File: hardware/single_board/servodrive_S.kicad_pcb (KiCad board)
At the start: 6 copper layers, 65 x 65 mm, 194 parts, among them J1 PhasePad_Arc, J12 USB-C, J13 EXPANSION, J14 RS485 IN, J15 RS485 OUT, J2 PhasePad_Arc, J3 PhasePad_Arc, J4 XT30, Q1 BSC030N08NS5, Q1001 2N7002, Q2 BSC030N08NS5, Q3 BSC030N08NS5, Q4 BSC030N08NS5, Q5 BSC030N08NS5, Q6 BSC030N08NS5, SW1 BOOTSEL, U1 EG2103, U10 MT6701, U11 LMR38010SDDAR, U12 LMR38010SDDAR, U13 USBLC6-2SC6, U14 SIT3088ETK, U15 SIT3088ETK, U17 SIT3088ETK, U18 SIT3088ETK, U2 EG2103, U3 EG2103, U4 INA241A3, U5 INA241A3, U6 INA241A3, U7 RP2350A, U8 W25Q16JVUXIQ, U9 SPX3819M5-3.3, Y1 12MHz

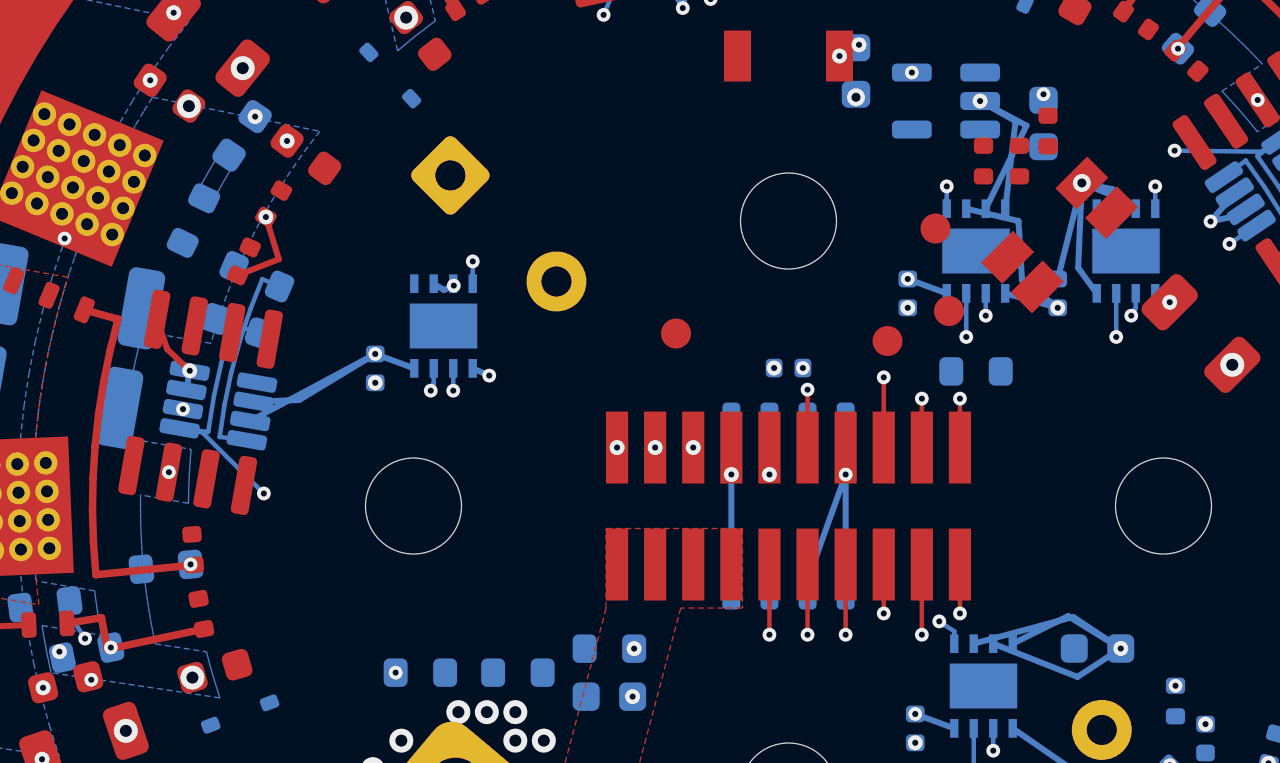
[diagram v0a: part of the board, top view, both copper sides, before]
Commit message: fanout.taps: no sliver where a pad joins a neighbour's tap
J13's pin swap put EXP_GP24 on the pad above the MT6701's pin 2, so
that pin lost its via-in-pad and linked to pin 1's tap via instead: two
+3V3 tracks meeting at 19.8 degrees, a copper sliver in KiCad's DRC.
A link that would arrive at a via at 2-20 degrees to a track running
from it to one of the net's pads now goes straight to that pad. On
board S that changes U10 pins 1-2 and one +3V3 pair at (157.8, 94.2)
(11.6 degrees); board A's fan-out is unchanged.

Co-Authored-By: Claude Opus 5.5 (1M context) <noreply@anthropic.com>
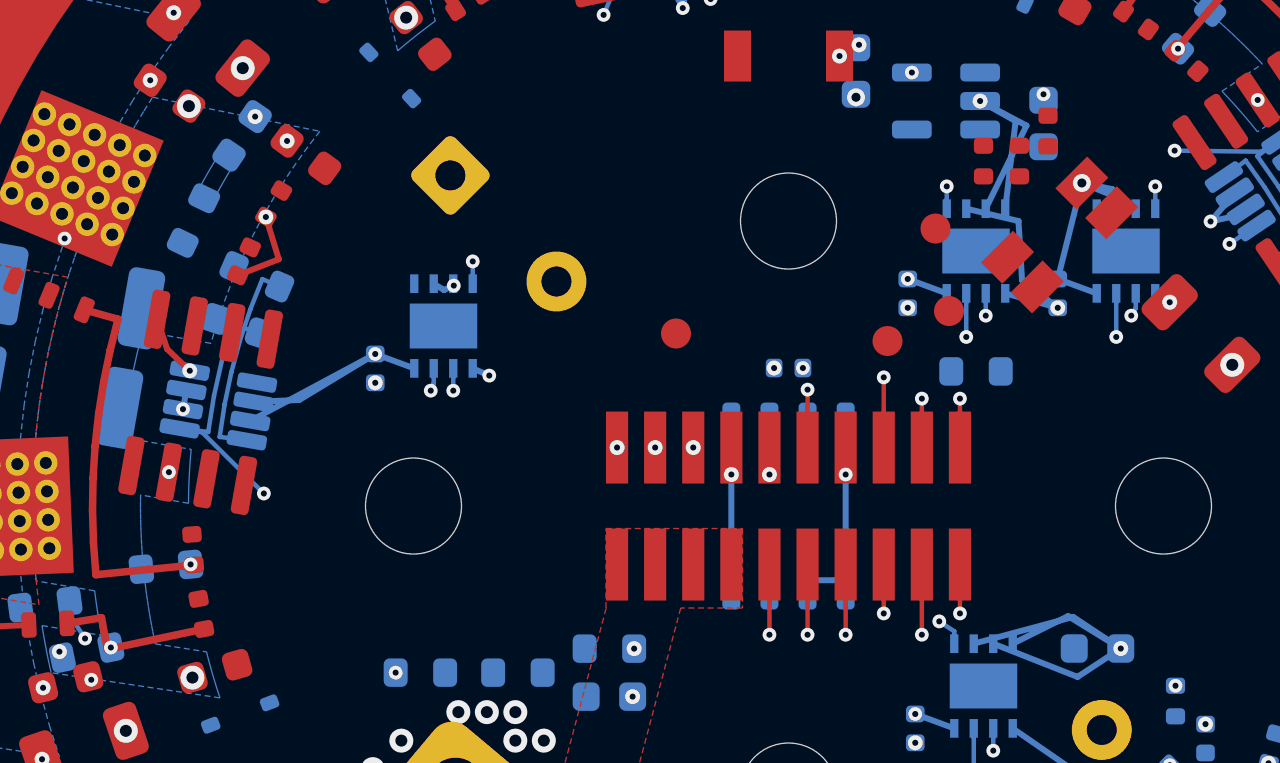
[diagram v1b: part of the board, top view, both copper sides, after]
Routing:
- net +3V3: track 64.0 -> 59.0 mm

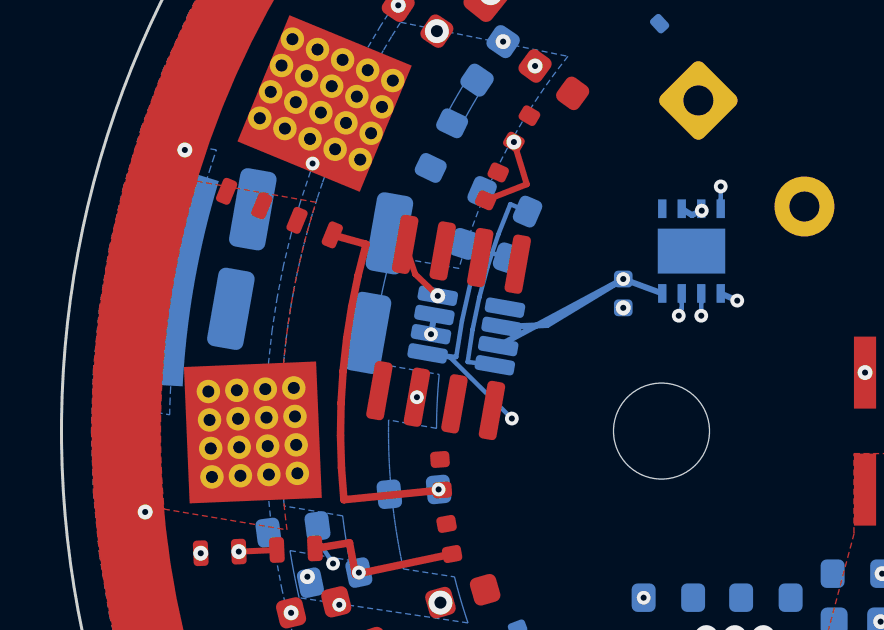
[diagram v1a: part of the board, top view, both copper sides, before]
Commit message: Board S: GATE_OFF and FAULT_n to GPIO2/3, port OUT's PIO UART to 14/15 (unrouted)
On GPIO14/15, GATE_OFF and FAULT_n left the RP2350 on the side facing away
from Q1001 and R705; with keepouts round the motor screws that side's
corridor was one track short, and every router and rip-up left one of
GATE_OFF, FAULT_n, RUN or LED_R open. GPIO0-3 are the pads nearest Q1001,
and port OUT's transceivers sit on 14/15's side. A PIO UART takes any
pins; GPIO2 is pulled down through reset as 14 was, so the gate rail still
comes up braking.

Board regenerated, not yet routed. Netlist check, KiCad netlist export and
ERC clean.

Co-Authored-By: Claude Opus 5.5 (1M context) <noreply@anthropic.com>
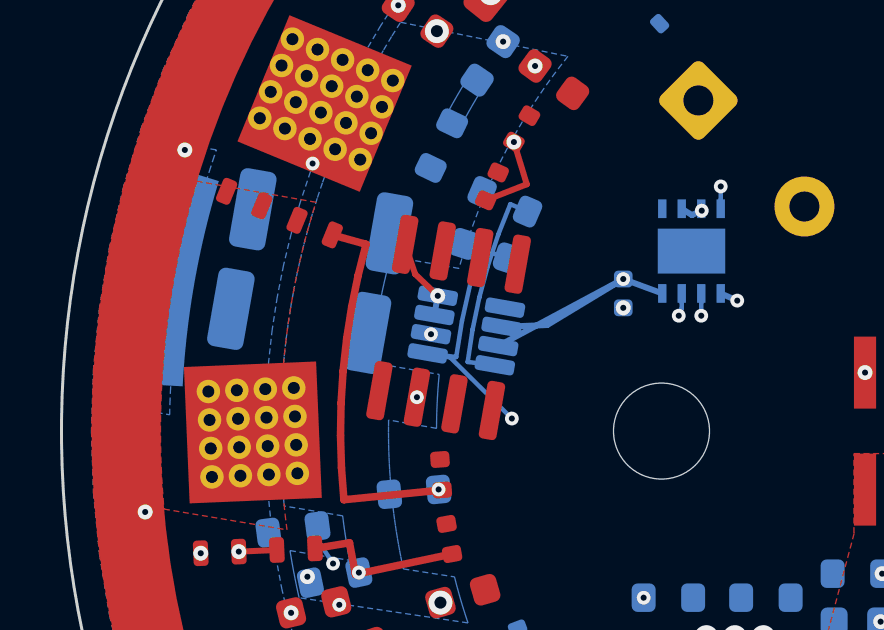
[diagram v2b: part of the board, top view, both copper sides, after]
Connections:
- U7 pad 18: GATE_OFF -> RS485_OUT_TX
- U7 pad 19: FAULT_n -> RS485_OUT_RX
- U7 pad 4: RS485_OUT_TX -> GATE_OFF
- U7 pad 5: RS485_OUT_RX -> FAULT_n
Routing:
- net RS485_OUT_RX: track 3.89 -> 3.01 mm
- net FAULT_n: track 2.26 -> 3.15 mm
- net GATE_OFF: track 3.20 -> 3.88 mm
- net RS485_OUT_TX: track 4.62 -> 3.94 mm
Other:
- board text added: "Board A plus the minimum of board B. 48 V max. XT30 bus input, TVS and cans, two LMR38010 rails, USB-C, RS-485 relay on two SH 6, expansion header."
- board text removed: "Board A plus the minimum of board B. 48 V max. Bus pads, TVS and cans, two LMR38010 rails, USB-C, RS-485 relay on two SH 6, expansion header."

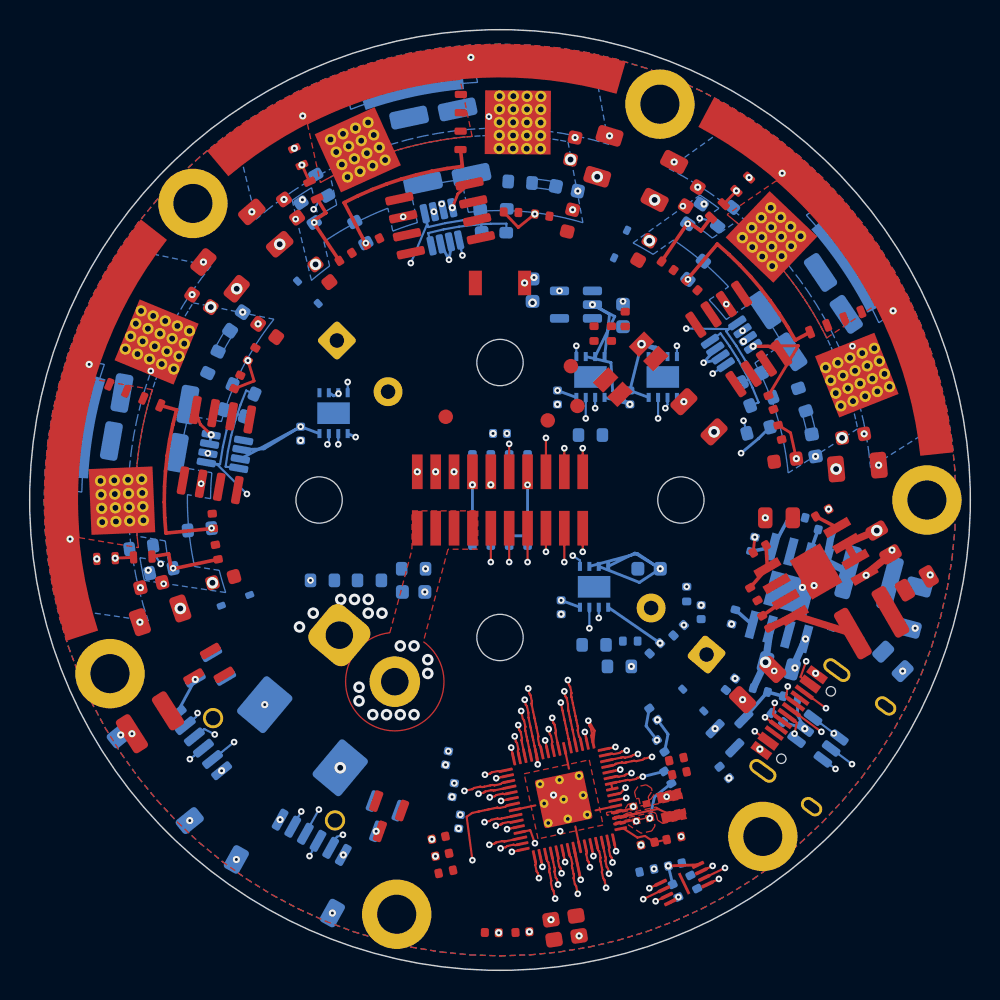
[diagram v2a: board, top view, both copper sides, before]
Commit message: Board S routed with GATE_OFF/FAULT_n on GPIO2/3: 0 unconnected, DRC 0
route.py --rounds 1 --first EN_12V,USB_VBUS,LIN_A,EXP_GP19,EXP_GP22 left one
connection, ENC_OUT; a targeted rip-up (ENC_DO and RS485_IN_DN_P out of the
way, ENC_OUT made, both made again) closed it. The router's +5V via beside
the 5 V buck's SW link was 0.24 mm from it against the Phase class's 0.4:
moved 0.3 mm clear. Dangling vias dropped, polished.

1958 track segments, 418 vias; DRC 0 at every severity, 0 unconnected;
ERC 0; the board's pads against schematic_s.nets(): 714, none differ;
deadcheck 0; schematic parity unchanged (219, the same kinds as before).

Page and README: the new GPIO map, J13's pinout, the In3 fine-centre rule
and the screw keepouts; the encoder-pins open item is closed (SPI0).

Co-Authored-By: Claude Opus 5.5 (1M context) <noreply@anthropic.com>
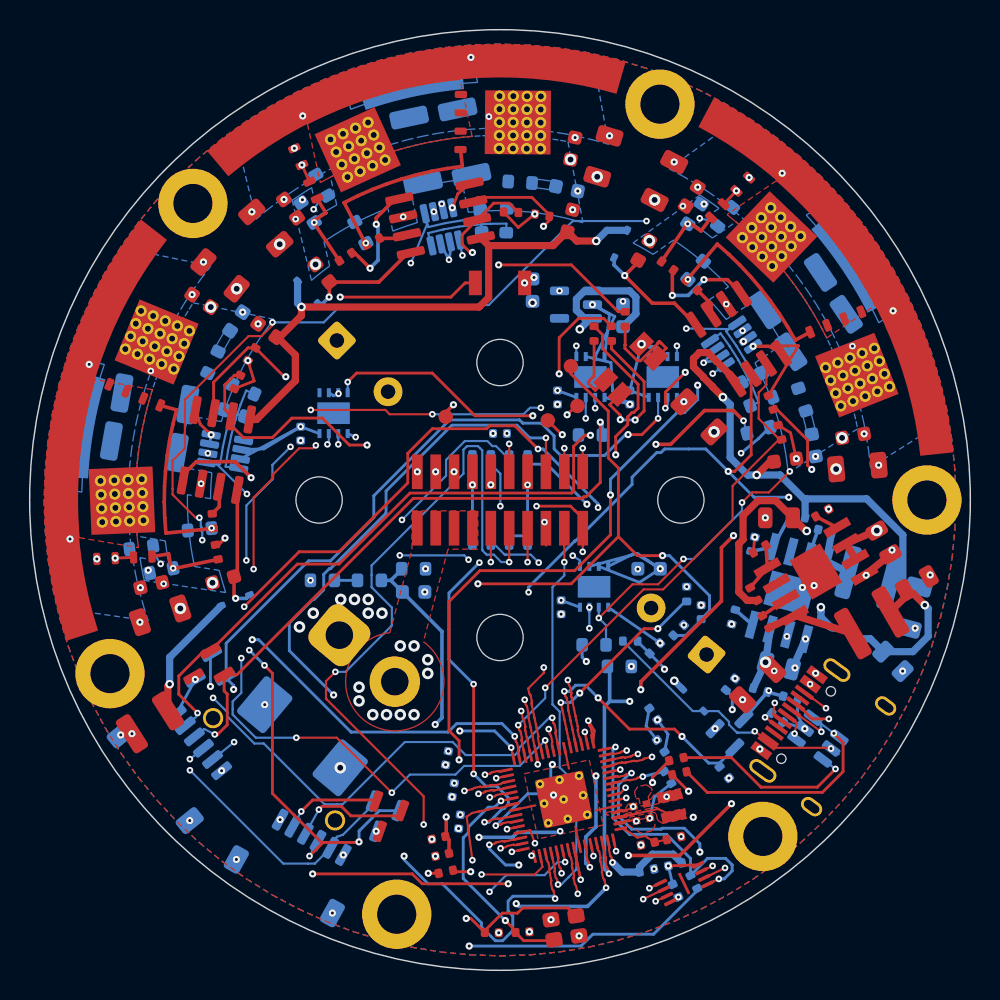
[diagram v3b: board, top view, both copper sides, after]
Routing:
- net +12V: track 0.00 -> 132.6 mm, vias 0 -> 5
- net RS485_IN_DN_P: track 2.06 -> 129.1 mm, vias 2 -> 9
- net LED_B: track 1.56 -> 84.9 mm, vias 1 -> 4
- net BOOTSEL: track 0.00 -> 81.7 mm, vias 0 -> 2
- net ISENSE_B: track 1.91 -> 83.5 mm, vias 2 -> 4
- net ENC_DO: track 2.26 -> 83.2 mm, vias 1 -> 8
- net RS485_OUT_DN_P: track 2.70 -> 79.4 mm, vias 2 -> 4
- net FET_TEMP: track 3.17 -> 75.0 mm, vias 2 -> 6
- net RS485_IN_DN_N: track 2.66 -> 73.3 mm, vias 2 -> 10
- net ENC_SCK: track 0.82 -> 69.1 mm, vias 1 -> 7
- net HIN_B: track 1.56 -> 67.9 mm, vias 1 -> 3
- net EXP_GP21: track 5.54 -> 66.4 mm, vias 2 -> 4
- net +5V: track 1.93 -> 61.9 mm, vias 1 -> 4
- net EXP_GP24: track 3.16 -> 61.8 mm, vias 2 -> 5
- net LED_G: track 2.26 -> 60.3 mm, vias 1 -> 3
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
